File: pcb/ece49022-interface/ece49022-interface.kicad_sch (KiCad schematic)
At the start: 8 parts, among them J2 Conn_01x04_Pin, J3 Conn_01x02_Pin, J4 Conn_01x03_Pin, J5 Conn_01x01_Pin, J6 Conn_01x01_Pin, J7 Conn_01x02_Pin

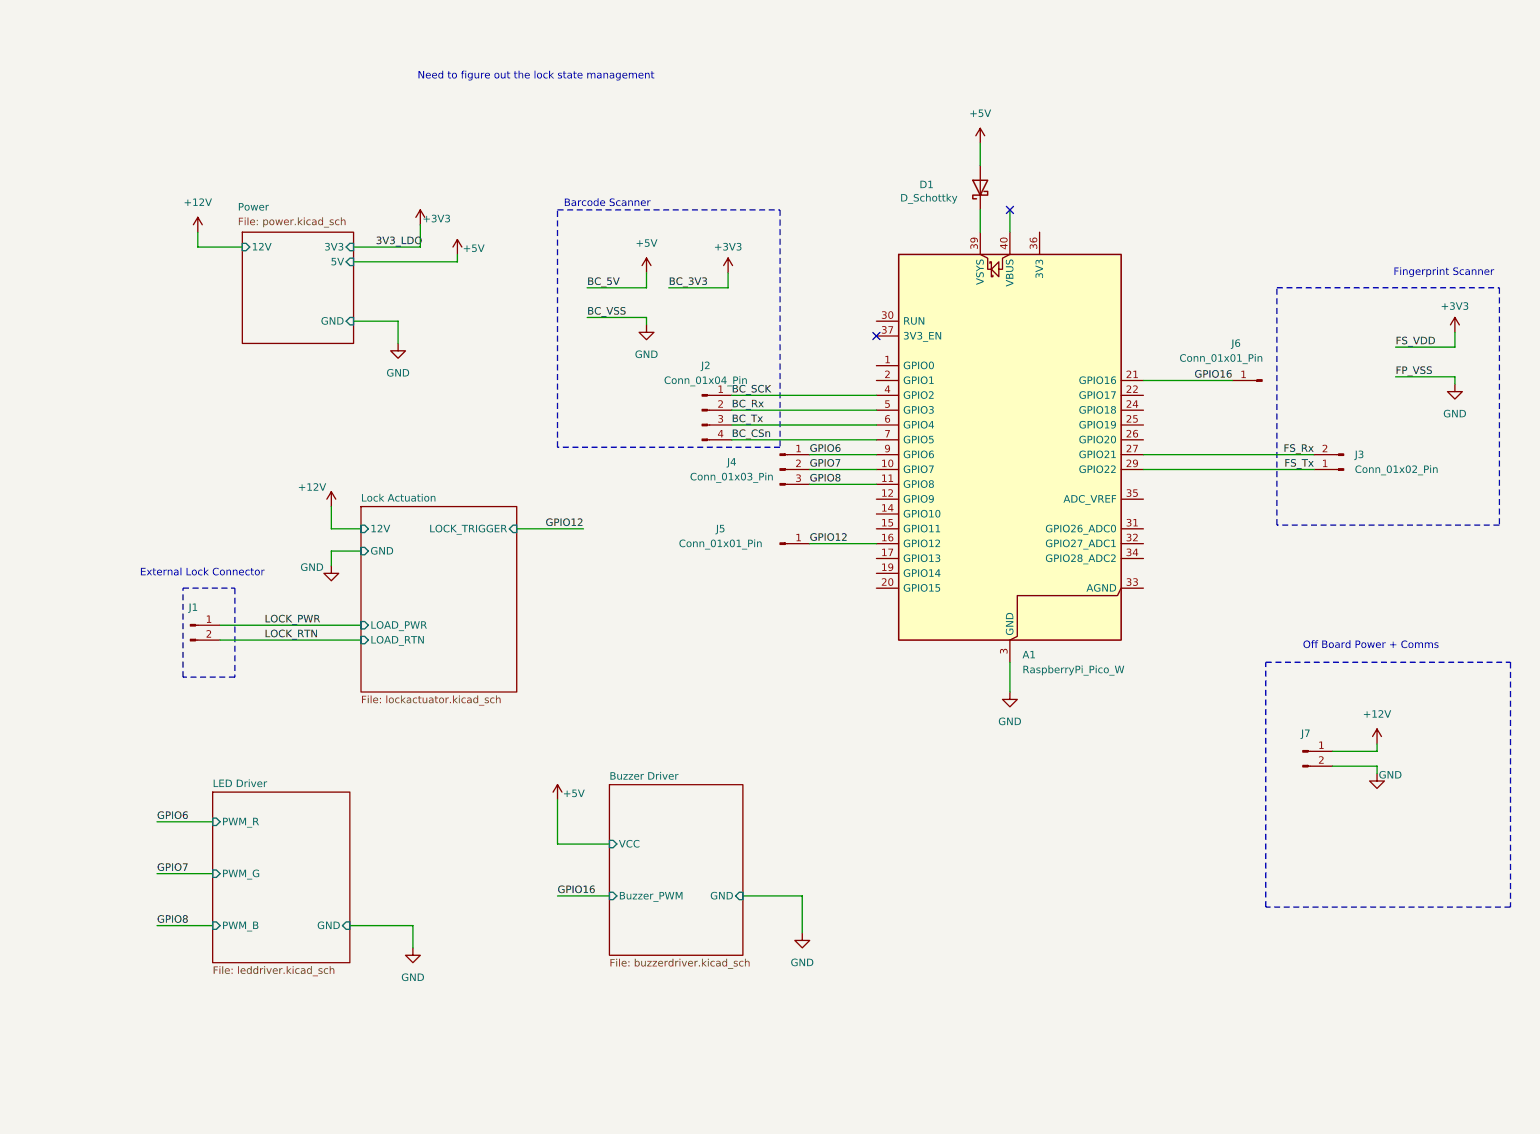
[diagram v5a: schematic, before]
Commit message: Redid external pin connectors
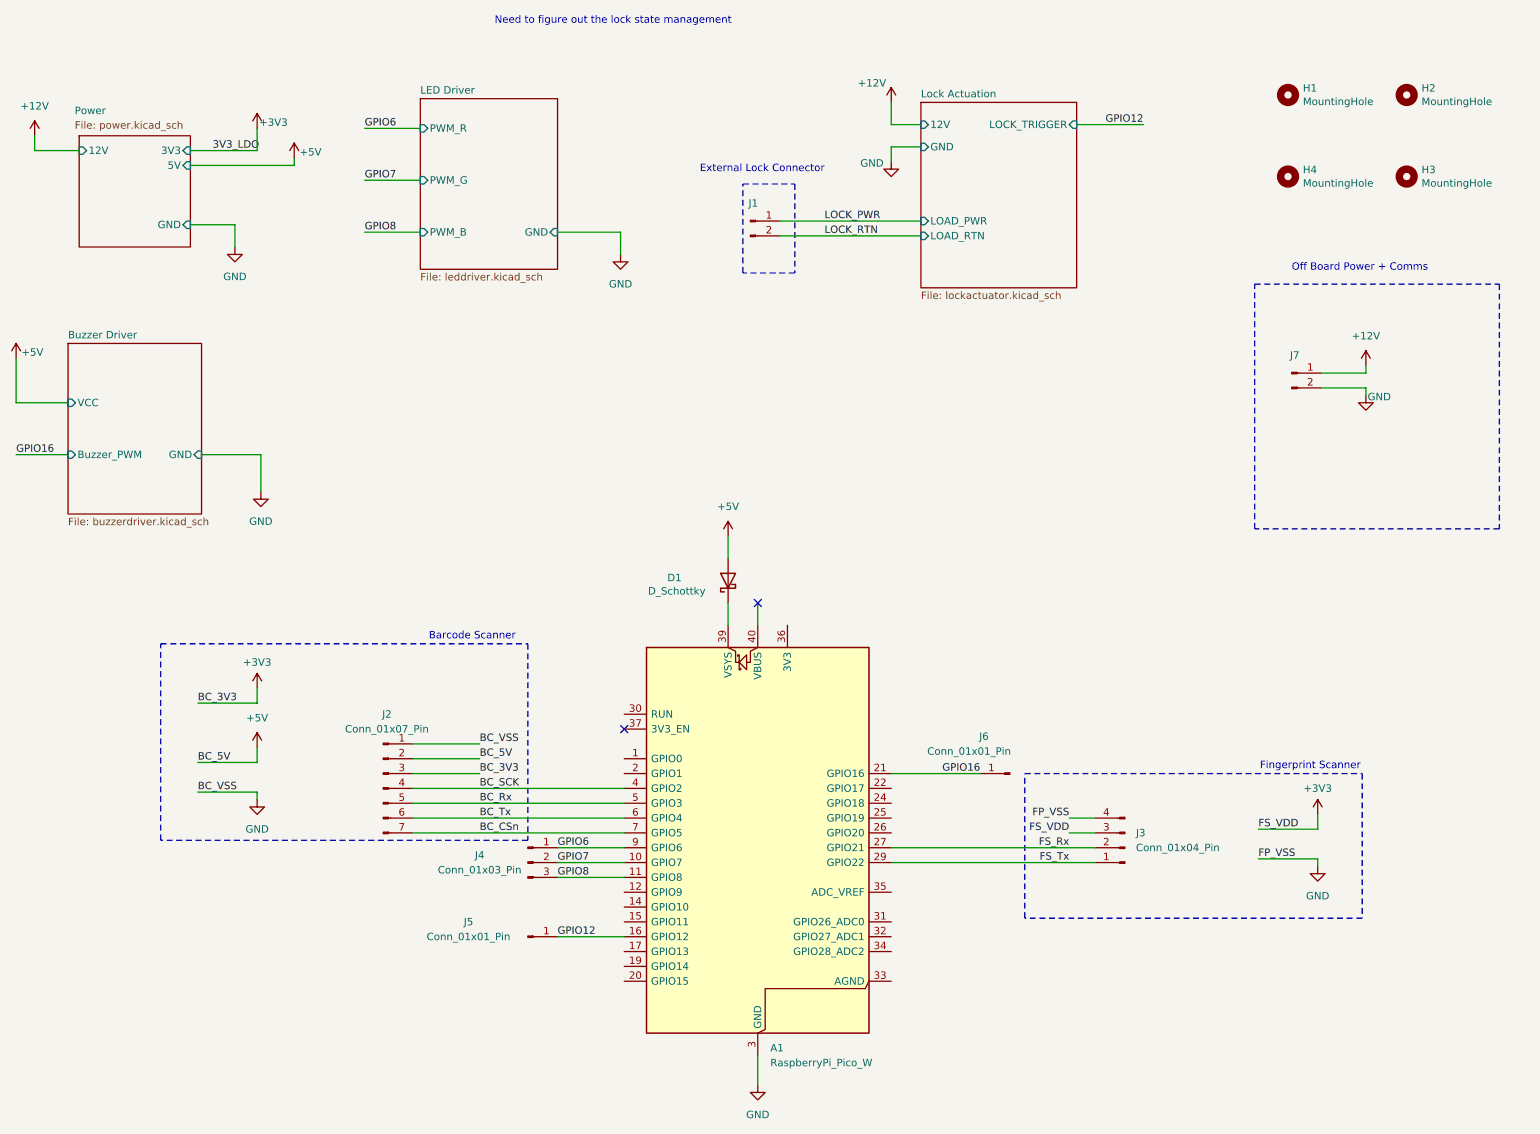
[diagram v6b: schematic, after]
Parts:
- removed J2: Conn_01x04_Pin, Connector_PinHeader_2.54mm:PinHeader_1x04_P2.54mm_Vertical, symbol Connector:Conn_01x04_Pin
- removed J3: Conn_01x02_Pin, Connector_PinHeader_2.54mm:PinHeader_1x02_P2.54mm_Vertical, symbol Connector:Conn_01x02_Pin
- added H1, H2, H3, H4: MountingHole, MountingHole:MountingHole_2.7mm_M2.5, symbol Mechanical:MountingHole
- added J2: Conn_01x07_Pin, Connector_PinHeader_2.54mm:PinHeader_1x07_P2.54mm_Vertical, symbol Connector:Conn_01x07_Pin
- added J3: Conn_01x04_Pin, Connector_PinHeader_2.54mm:PinHeader_1x04_P2.54mm_Vertical, symbol Connector:Conn_01x04_Pin
- J4: footprint Connector_PinHeader_2.54mm:PinHeader_1x03_P2.54mm_Vertical -> (none)
- J5: footprint Connector_PinHeader_2.54mm:PinHeader_1x01_P2.54mm_Vertical -> (none)
- renumbered J7 to J1
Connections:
- net +3V3: now also J2.3 (Pin_3), J3.3 (Pin_3)
- net +5V: now also J2.2 (Pin_2)
- net BC_CSn: now also J2.7 (Pin_7)
- net BC_Rx: now also J2.5 (Pin_5)
- net BC_SCK: now also J2.4 (Pin_4)
- net BC_Tx: now also J2.6 (Pin_6)
- net FS_Rx: now also J3.2 (Pin_2)
- net FS_Tx: now also J3.1 (Pin_1)
- net GND: now also J2.1 (Pin_1), J3.4 (Pin_4)
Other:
- moved on the sheet: A1, D1, J4, J5, J6, J7

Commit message: pcb in progress
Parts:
- removed J4: Conn_01x03_Pin, symbol Connector:Conn_01x03_Pin
- removed J5: Conn_01x01_Pin, symbol Connector:Conn_01x01_Pin
- added J1: Conn_01x03_Pin, Connector_PinHeader_2.54mm:PinHeader_1x03_P2.54mm_Vertical, symbol Connector:Conn_01x03_Pin
- renumbered J1 to J7
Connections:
- net GPIO12: now also J1.3 (Pin_3)
- net LOCK_PWR: now also J1.1 (Pin_1); no longer J7.1 (Pin_1)
- net LOCK_RTN: now also J1.2 (Pin_2); no longer J7.2 (Pin_2)
- no-connect marks 2 -> 20
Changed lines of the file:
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@@
 	(paper "A4")
 	(rectangle
-		(start 142.875 34.925)
-		(end 151.765 50.165)
+		(start 136.525 34.29)
+		(end 161.925 53.975)
 		(stroke
 			(width 0)
@@
 	)
 	(no_connect
+		(at 168.275 166.37)
+	)
+	(no_connect
+		(at 122.555 135.89)
+	)
+	(no_connect
 		(at 122.555 128.27)
 	)
 	(no_connect
+		(at 168.275 146.05)
+	)
+	(no_connect
+		(at 168.275 143.51)
+	)
+	(no_connect
+		(at 168.275 138.43)
+	)
+	(no_connect
+		(at 122.555 166.37)
+	)
+	(no_connect
+		(at 168.275 171.45)
+	)
+	(no_connect
+		(at 122.555 171.45)
+	)
+	(no_connect
+		(at 168.275 156.21)
+	)
+	(no_connect
+		(at 168.275 163.83)
+	)
+	(no_connect
 		(at 145.415 106.68)
 	)
-	(wire
-		(pts
-			(xy 200.025 24.765) (xy 211.455 24.765)
-		)
-		(stroke
-			(width 0)
-			(type default)
-		)
+	(no_connect
+		(at 122.555 161.29)
+	)
+	(no_connect
+		(at 168.275 161.29)
+	)
+	(no_connect
+		(at 168.275 140.97)
+	)
+	(no_connect
+		(at 122.555 133.35)
+	)
+	(no_connect
+		(at 122.555 156.21)
+	)
+	(no_connect
+		(at 122.555 125.73)
+	)
+	(no_connect
+		(at 122.555 158.75)
+	)
+	(no_connect
+		(at 122.555 168.91)
 	)
 	(wire
@@
 	(wire
 		(pts
+			(xy 149.225 46.355) (xy 173.355 46.355)
+		)
+		(stroke
+			(width 0)
+			(type default)
+		)
+	)
+	(wire
+		(pts
 			(xy 168.275 148.59) (xy 203.2 148.59)
 		)
@@
 	)
 	(label "LOCK_PWR"
-		(at 156.845 41.275 0)
+		(at 152.4 41.275 0)
 		(effects
 			(font
@@
 	)
 	(label "LOCK_RTN"
-		(at 156.845 43.815 0)
+		(at 152.4 43.815 0)
 		(effects
 			(font
@@
 	)
 	(label "GPIO12"
-		(at 211.455 24.765 180)
+		(at 152.4 46.355 0)
 		(effects
 			(font
 				(size 1.27 1.27)
 			)
-			(justify right bottom)
+			(justify left bottom)
 		)
 	)
@@
 	)
 	(symbol
-		(lib_id "Connector:Conn_01x03_Pin")
-		(at 106.045 151.13 0)
-		(unit 1)
-		(exclude_from_sim no)
-		(in_bom yes)
-		(on_board yes)
-		(dnp no)
-		(property "Reference" "J4"
-			(at 97.79 149.86 0)
-			(effects
-				(font
-					(size 1.27 1.27)
-				)
-			)
-		)
-		(property "Value" "Conn_01x03_Pin"
-			(at 97.79 152.4 0)
-			(effects
-				(font
-					(size 1.27 1.27)
-				)
-			)
-		)
-		(property "Footprint" ""
-			(at 106.045 151.13 0)
-			(effects
-				(font
-					(size 1.27 1.27)
-				)
-				(hide yes)
-			)
-		)
-		(property "Datasheet" "~"
-			(at 106.045 151.13 0)
-			(effects
-				(font
-					(size 1.27 1.27)
-				)
-				(hide yes)
-			)
-		)
-		(property "Description" "Generic connector, single row, 01x03, script generated"
-			(at 106.045 151.13 0)
-			(effects
-				(font
-					(size 1.27 1.27)
-				)
-				(hide yes)
-			)
-		)
-		(pin "3"
-		)
-		(pin "1"
-		)
-		(pin "2"
-		)
-		(instances
-			(project ""
-				(path "/ad062fbe-cbe6-4ffd-876d-97a59a1c7176"
-					(reference "J4")
-					(unit 1)
-				)
-			)
-		)
-	)
-	(symbol
 		(lib_id "Mechanical:MountingHole")
 		(at 256.54 33.655 0)
@@
 	)
 	(symbol
+		(lib_id "Connector:Conn_01x03_Pin")
+		(at 144.145 43.815 0)
+		(unit 1)
+		(exclude_from_sim no)
+		(in_bom yes)
+		(on_board yes)
+		(dnp no)
+		(property "Reference" "J1"
+			(at 145.415 35.56 0)
+			(effects
+				(font
+					(size 1.27 1.27)
+				)
+			)
+		)
+		(property "Value" "Conn_01x03_Pin"
+			(at 145.415 38.1 0)
+			(effects
+				(font
+					(size 1.27 1.27)
+				)
+			)
+		)
+		(property "Footprint" "Connector_PinHeader_2.54mm:PinHeader_1x03_P2.54mm_Vertical"
+			(at 144.145 43.815 0)
+			(effects
+				(font
+					(size 1.27 1.27)
+				)
+				(hide yes)
+			)
+		)
+		(property "Datasheet" "~"
+			(at 144.145 43.815 0)
+			(effects
+				(font
+					(size 1.27 1.27)
+				)
+				(hide yes)
+			)
+		)
+		(property "Description" "Generic connector, single row, 01x03, script generated"
+			(at 144.145 43.815 0)
+			(effects
+				(font
+					(size 1.27 1.27)
+				)
+				(hide yes)
+			)
+		)
+		(pin "1"
+		)
+		(pin "2"
+		)
+		(pin "3"
+		)
+		(instances
+			(project ""
+				(path "/ad062fbe-cbe6-4ffd-876d-97a59a1c7176"
+					(reference "J1")
+					(unit 1)
+				)
+			)
+		)
+	)
+	(symbol
 		(lib_id "power:GND")
 		(at 168.275 31.115 0)
@@
 	)
 	(symbol
-		(lib_id "Connector:Conn_01x02_Pin")
-		(at 144.145 41.275 0)
-		(unit 1)
-		(exclude_from_sim no)
-		(in_bom yes)
-		(on_board yes)
-		(dnp no)
-		(property "Reference" "J1"
-			(at 144.653 38.227 0)
-			(effects
-				(font
-					(size 1.27 1.27)
-				)
-			)
-		)
-		(property "Value" "Conn_01x02_Pin"
-			(at 144.78 38.735 0)
-			(effects
-				(font
-					(size 1.27 1.27)
-				)
-				(hide yes)
-			)
-		)
-		(property "Footprint" "Connector_PinHeader_2.54mm:PinHeader_1x02_P2.54mm_Vertical"
-			(at 144.145 41.275 0)
-			(effects
-				(font
-					(size 1.27 1.27)
-				)
-				(hide yes)
-			)
-		)
-		(property "Datasheet" "~"
-			(at 144.145 41.275 0)
-			(effects
-				(font
-					(size 1.27 1.27)
-				)
-				(hide yes)
-			)
-		)
-		(property "Description" "Generic connector, single row, 01x02, script generated"
-			(at 144.145 41.275 0)
-			(effects
-				(font
-					(size 1.27 1.27)
-				)
-				(hide yes)
-			)
-		)
-		(pin "2"
-		)
-		(pin "1"
-		)
-		(instances
-			(project "ece49022-interface"
-				(path "/ad062fbe-cbe6-4ffd-876d-97a59a1c7176"
-					(reference "J1")
-					(unit 1)
-				)
-			)
-		)
-	)
-	(symbol
 		(lib_id "power:+5V")
 		(at 59.69 121.285 0)
@@
 	)
 	(symbol
-		(lib_id "Connector:Conn_01x01_Pin")
-		(at 106.045 163.83 0)
-		(unit 1)
-		(exclude_from_sim no)
-		(in_bom yes)
-		(on_board yes)
-		(dnp no)
-		(property "Reference" "J5"
-			(at 95.885 161.29 0)
-			(effects
-				(font
-					(size 1.27 1.27)
-				)
-			)
-		)
-		(property "Value" "Conn_01x01_Pin"
-			(at 95.885 163.83 0)
-			(effects
-				(font
-					(size 1.27 1.27)
-				)
-			)
-		)
-		(property "Footprint" ""
-			(at 106.045 163.83 0)
-			(effects
-				(font
-					(size 1.27 1.27)
-				)
-				(hide yes)
-			)
-		)
-		(property "Datasheet" "~"
-			(at 106.045 163.83 0)
-			(effects
-				(font
-					(size 1.27 1.27)
-				)
-				(hide yes)
-			)
-		)
-		(property "Description" "Generic connector, single row, 01x01, script generated"
-			(at 106.045 163.83 0)
-			(effects
-				(font
-					(size 1.27 1.27)
-				)
-				(hide yes)
-			)
-		)
-		(pin "1"
-		)
-		(instances
-			(project ""
-				(path "/ad062fbe-cbe6-4ffd-876d-97a59a1c7176"
-					(reference "J5")
-					(unit 1)
-				)
-			)
-		)
-	)
-	(symbol
 		(lib_id "Mechanical:MountingHole")
 		(at 256.54 19.685 0)
@@
 		)
 		(pin "LOCK_TRIGGER" input
-			(at 200.025 24.765 0)
+			(at 173.355 46.355 180)
 			(effects
 				(font
 					(size 1.27 1.27)
 				)
-				(justify right)
+				(justify left)
 			)
 		)

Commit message: update for pcb
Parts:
- removed J2: Conn_01x07_Pin, Connector_PinHeader_2.54mm:PinHeader_1x07_P2.54mm_Vertical, symbol Connector:Conn_01x07_Pin
- removed J6: Conn_01x01_Pin, Connector_PinHeader_2.54mm:PinHeader_1x01_P2.54mm_Vertical, symbol Connector:Conn_01x01_Pin
- added J2: Conn_01x05_Pin, Connector_PinHeader_2.54mm:PinHeader_1x05_P2.54mm_Vertical, symbol Connector:Conn_01x05_Pin
- added J4: Conn_01x04_Pin, Connector_PinHeader_2.54mm:PinHeader_1x04_P2.54mm_Vertical, symbol Connector:Conn_01x04_Pin
- added J5: Conn_01x02_Pin, Connector_PinHeader_2.54mm:PinHeader_1x02_P2.54mm_Vertical, symbol Connector:Conn_01x02_Pin
- added R4, R5, R6: 47, 1%, Resistor_SMD:R_0402_1005Metric_Pad0.72x0.64mm_HandSolder, symbol Device:R_US
- renumbered J7 to J6
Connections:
- net GPIO16 is gone; now on net FS_Rx: A1.21 (GPIO16)
- net +3V3: now also J3.2 (Pin_2), J2.2 (Pin_2); no longer J3.3 (Pin_3)
- net +5V: now also J2.3 (Pin_3)
- net BC_Rx: now also A1.16 (GPIO12), J2.4 (Pin_4); no longer A1.5 (GPIO3)
- net BC_Tx: now also A1.17 (GPIO13), J2.5 (Pin_5); no longer A1.6 (GPIO4)
- net FS_Rx: now also J3.4 (Pin_4); no longer A1.27 (GPIO21), J3.2 (Pin_2)
- net FS_Tx: now also A1.22 (GPIO17), J3.3 (Pin_3); no longer A1.29 (GPIO22), J3.1 (Pin_1)
- net GND: now also J3.1 (Pin_1), J2.1 (Pin_1), J4.1 (Pin_1); no longer J3.4 (Pin_4)
- net GPIO18: now reaches A1.24 (GPIO18)
- net MAIN_MCU_I2C_SDA: now reaches A1.26 (GPIO20)
- net MAIN_MCU_I2C_SDA: now also J5.1 (Pin_1)
- net BC_CSn: no longer names the net of A1.7 (GPIO5)
- net BC_SCK: no longer names the net of A1.4 (GPIO2)
- net BC_SCK: now also R4.2
- net GPIO12 renamed GPIO22
- net GPIO22: now also A1.29 (GPIO22); no longer A1.16 (GPIO12)
- net GPIO6: no longer names the net of A1.9 (GPIO6)
- net GPIO7: no longer names the net of A1.10 (GPIO7)
- net GPIO8: no longer names the net of A1.11 (GPIO8)
- new net: A1.6 (GPIO4), R6.2
- new net: A1.5 (GPIO3), R5.2
- new net MAIN_MCU_I2C_SCL: A1.27 (GPIO21), J5.2 (Pin_2)
- new net PWM_B: J4.4 (Pin_4), R6.1
- new net PWM_G: J4.3 (Pin_3), R5.1
- new net PWM_R: J4.2 (Pin_2), R4.1
- no-connect marks 20 -> 15
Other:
- removed sheet LED Driver
- note added: "RGB LED"
- moved on the sheet: H1, H2, H3, H4, J1, J3, J6
